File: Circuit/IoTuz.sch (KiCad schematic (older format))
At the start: 29 parts, among them P1 Alligator Connector, P2 BATTERY, P3 USB_5PIN_SHELL, P4 LED_1, P5 LED_2, P6 CONN_01X20, P7 CONN_01X20, Q1 S8050, Q2 S8050, Q3 FDN340P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

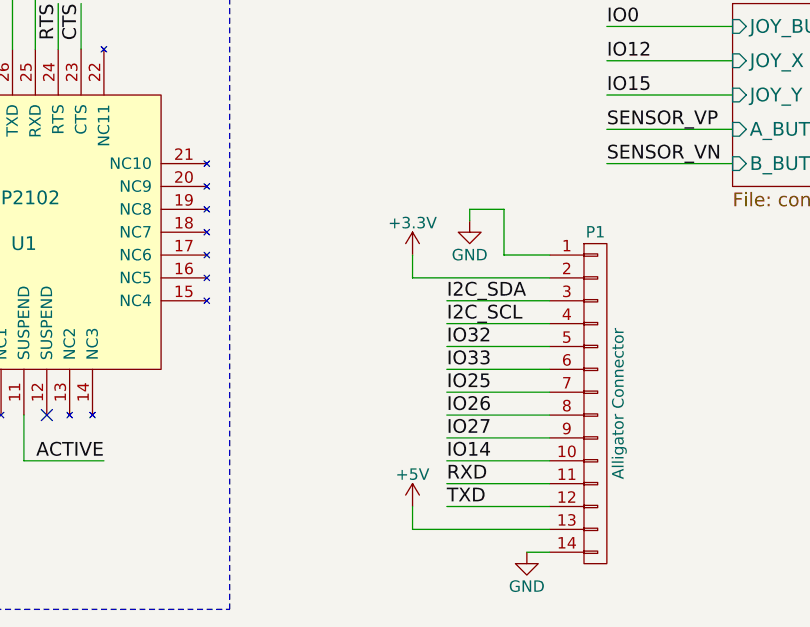
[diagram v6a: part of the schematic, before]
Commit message: Mounting points. Need to add for LCD as well.
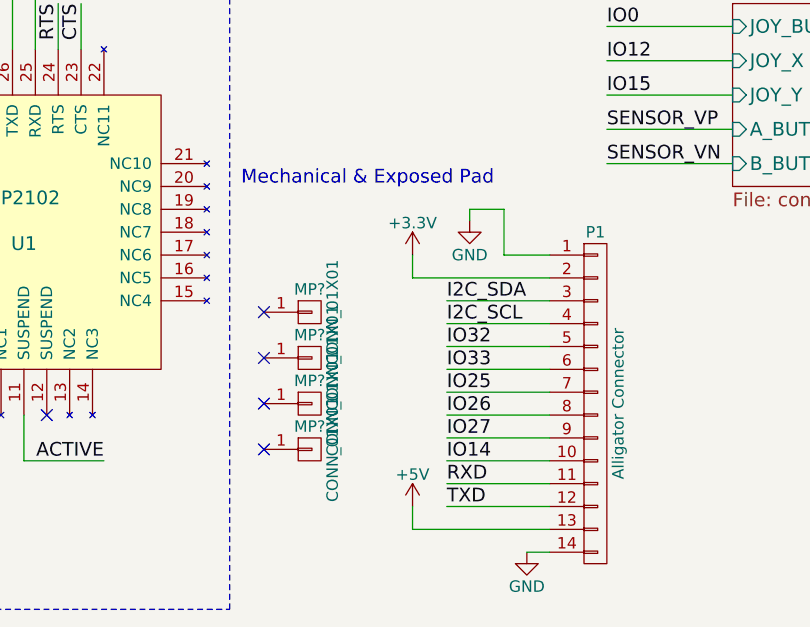
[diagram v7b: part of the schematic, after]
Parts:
- added MP? (x4): CONN_01X01, Mounting_Holes:MountingHole_3.2mm_M3, symbol CONN_01X01
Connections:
- no-connect marks 6 -> 10
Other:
- note added: "Mechanical & Exposed Pad"
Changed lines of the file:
@@
 Text Notes 9250 3600 0    197  ~ 0
 REMOVE?
+$Comp
+L CONN_01X01 MP?
+U 1 1 5823739A
+P 5050 6550
+F 0 "MP?" H 5050 6650 50  0000 C CNN
+F 1 "CONN_01X01" V 5150 6550 50  0000 C CNN
+F 2 "Mounting_Holes:MountingHole_3.2mm_M3" H 5050 6550 50  0001 C CNN
+F 3 "" H 5050 6550 50  0000 C CNN
+	1    5050 6550
+	1    0    0    -1
+$EndComp
+NoConn ~ 4850 6550
+$Comp
+L CONN_01X01 MP?
+U 1 1 582394EA
+P 5050 6750
+F 0 "MP?" H 5050 6850 50  0000 C CNN
+F 1 "CONN_01X01" V 5150 6750 50  0000 C CNN
+F 2 "Mounting_Holes:MountingHole_3.2mm_M3" H 5050 6750 50  0001 C CNN
+F 3 "" H 5050 6750 50  0000 C CNN
+	1    5050 6750
+	1    0    0    -1
+$EndComp
+NoConn ~ 4850 6750
+$Comp
+L CONN_01X01 MP?
+U 1 1 58239739
+P 5050 6950
+F 0 "MP?" H 5050 7050 50  0000 C CNN
+F 1 "CONN_01X01" V 5150 6950 50  0000 C CNN
+F 2 "Mounting_Holes:MountingHole_3.2mm_M3" H 5050 6950 50  0001 C CNN
+F 3 "" H 5050 6950 50  0000 C CNN
+	1    5050 6950
+	1    0    0    -1
+$EndComp
+NoConn ~ 4850 6950
+$Comp
+L CONN_01X01 MP?
+U 1 1 58239740
+P 5050 7150
+F 0 "MP?" H 5050 7250 50  0000 C CNN
+F 1 "CONN_01X01" V 5150 7150 50  0000 C CNN
+F 2 "Mounting_Holes:MountingHole_3.2mm_M3" H 5050 7150 50  0001 C CNN
+F 3 "" H 5050 7150 50  0000 C CNN
+	1    5050 7150
+	1    0    0    -1
+$EndComp
+NoConn ~ 4850 7150
+Text Notes 4750 6000 0    60   ~ 0
+Mechanical & Exposed Pad
 $EndSCHEMATC
